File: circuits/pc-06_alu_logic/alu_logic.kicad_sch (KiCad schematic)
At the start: 20 parts, among them J1 Conn_01x10, U1 74HC244 driver1, U10 gatesB, U2 notL, U3 iorL, U4 primL, U5 74HC244 driver2, U6 gatesA, U7 notH, U8 iorH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

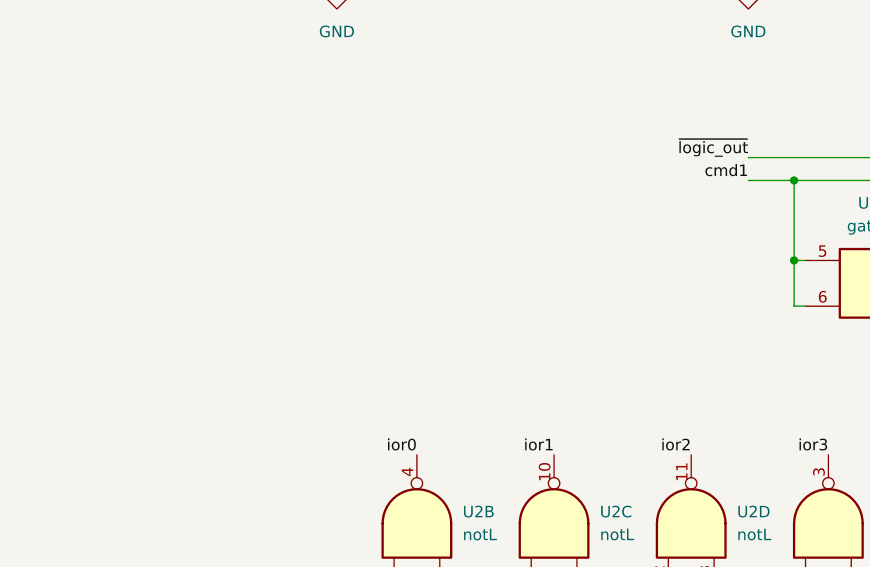
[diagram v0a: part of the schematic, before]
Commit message: add filter and decoupling capacitors to all boards
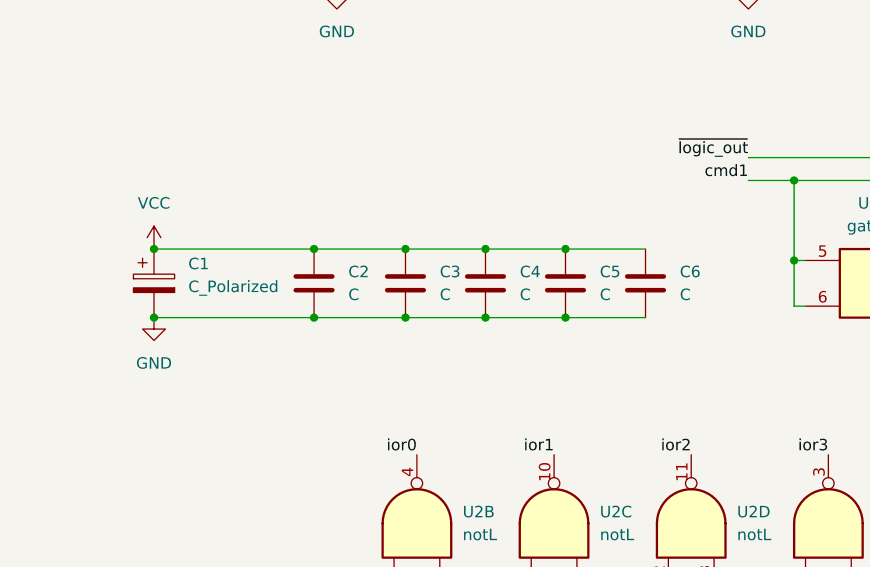
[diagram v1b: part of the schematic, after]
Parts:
- added C1: C_Polarized, Capacitor_SMD:CP_Elec_5x5.3, symbol Device:C_Polarized
- added C2, C3, C4, C5, C6: C, Capacitor_SMD:C_0603_1608Metric, symbol Device:C
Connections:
- net GND: now also C1.2, C2.2, C3.2, C4.2, C5.2, C6.2
- net VCC: now also C1.1, C2.1, C3.1, C4.1, C5.1, C6.1
